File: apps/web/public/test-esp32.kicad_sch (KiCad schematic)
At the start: 9 parts, among them J1 USB_5V, SW1 EN_BTN, U1 ESP32-WROOM-32, U2 AMS1117-3.3

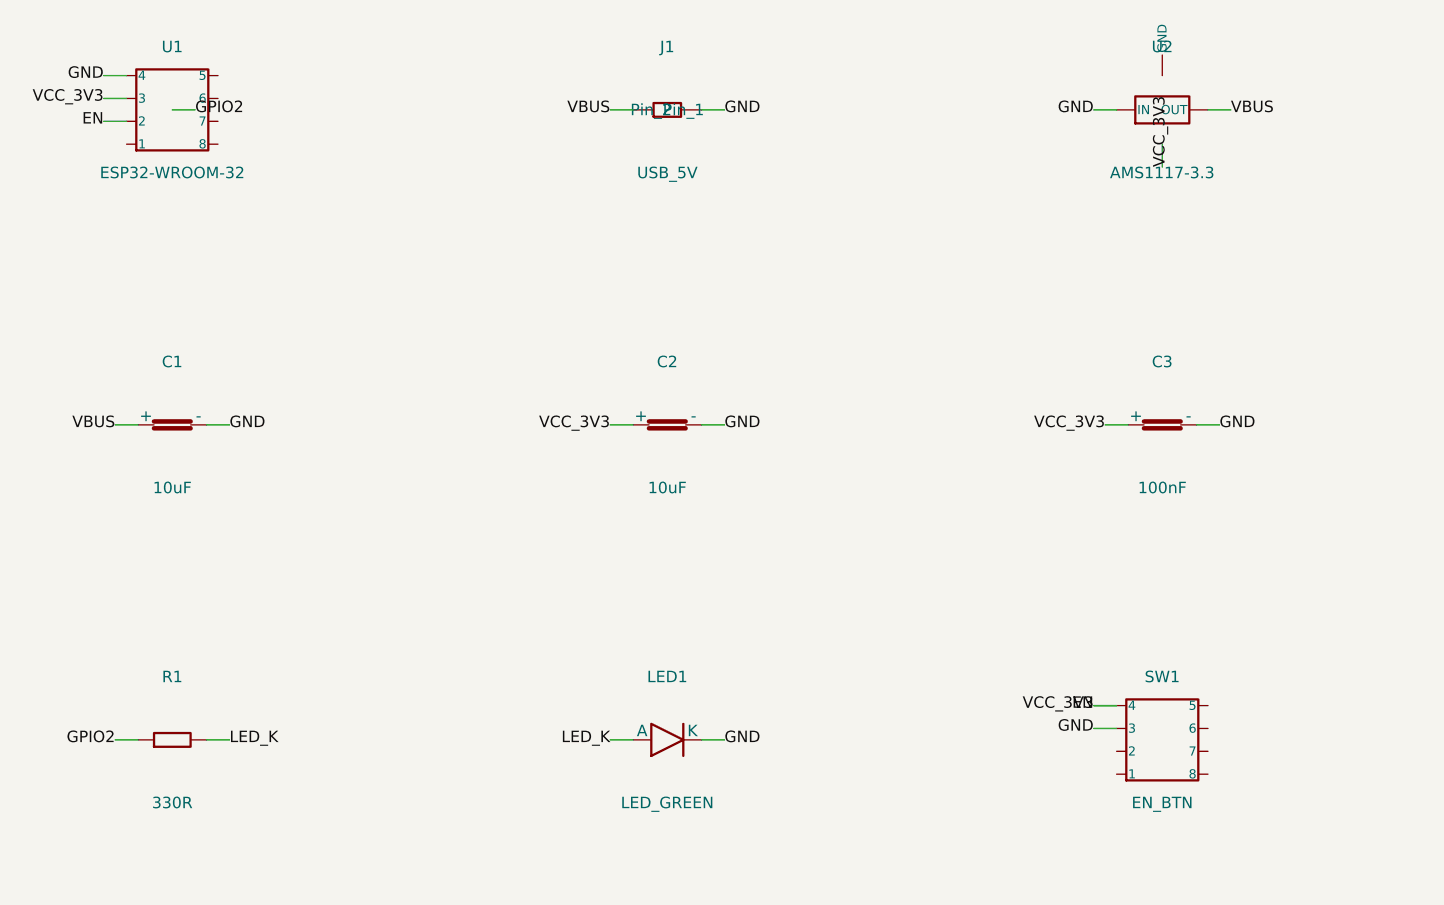
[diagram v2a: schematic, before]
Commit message: fix(layout): margin_top 12→20mm — composants 15mm du bord cadre interne
Composants étaient à y=12mm (7mm du bord interne), visuellement collés au cadre.
Maintenant à y=20mm (15mm de marge), clairement à l'intérieur du cadre.

- circuit_synth.py: margin_top = 20mm
- test-lm7805.kicad_sch: paper 149x123 (was 115)
- test-ne555.kicad_sch: paper 149x158 (was 150)
- test-esp32.kicad_sch: paper 149x158 (was 150)
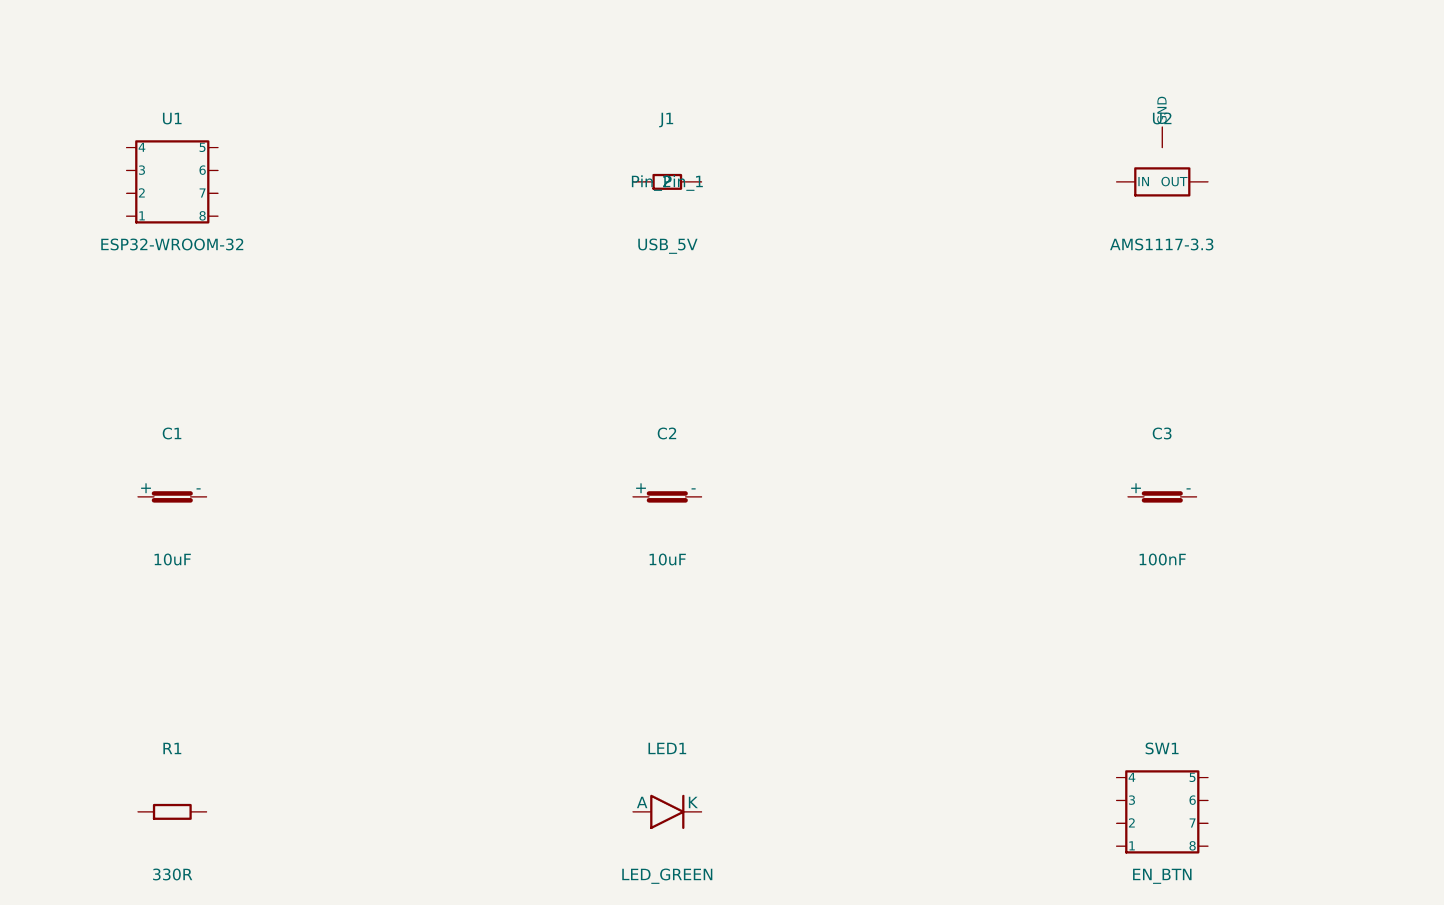
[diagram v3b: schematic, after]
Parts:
- C1, C2: footprint Capacitor_SMD:C_0805_2012Metric -> Capacitor_THT:C_Disc_D5.0mm_W2.5mm_P5.00mm
- C3: footprint Capacitor_SMD:C_0603_1608Metric -> Capacitor_THT:C_Disc_D5.0mm_W2.5mm_P5.00mm
- J1: footprint Connector_PinHeader_2.54mm:PinHeader_1x02_P2.54mm_Vertical -> Connector_USB:USB_B_Micro
- LED1: footprint LED_SMD:LED_0603_1608Metric -> LED_THT:LED_D5.0mm
- R1: footprint Resistor_SMD:R_0603_1608Metric -> Resistor_THT:R_Axial_DIN0207_L6.3mm_D2.5mm_P10.16mm_Horizontal
- SW1: footprint Button_Switch_SMD:SW_SPST_B3U-1000P -> Button_Switch_THT:SW_PUSH_6mm
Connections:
- removed net EN: C2.1 (+), C3.1 (+), SW1.4, U1.2, U1.3
- removed net GND: C1.2 (-), C2.2 (-), C3.2 (-), J1.2 (Pin_2), LED1.2 (K), SW1.3, U1.4, U2.1 (IN)
- net GPIO2: no longer names the net of R1.1
- net LED_K: no longer names the net of LED1.1 (A)
- net LED_K: no longer R1.2
- removed net VBUS: C1.1 (+), J1.1 (Pin_1), U2.3 (OUT)

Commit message: fix(schematic): add 20mm side margin to clear inner frame border
Components U1/J1 (left column) and far-right components were drawn
on top of the KiCad inner frame vertical borders (at x=10mm from
paper edge). The previous 12mm margin_side only gave 2mm clearance.

Changes:
- margin_side 12 -> 20mm in _build_flat_schematic_with_net_labels()
  (gives 10mm clearance from inner frame on both sides)
- Regenerated test-lm7805 / test-ne555 / test-esp32 .kicad_sch via
  /circuit-synth/generate (paper width 149 -> 165mm as a result)
- test-cs.html: ResizeObserver on canvas + window load/resize retries
  to reapply auto-zoom when KiCanvas resets its camera on layout
  changes (fixes title block peeking before click-to-interact)

Verified via Chrome DevTools screenshots on all 3 schematic tabs.
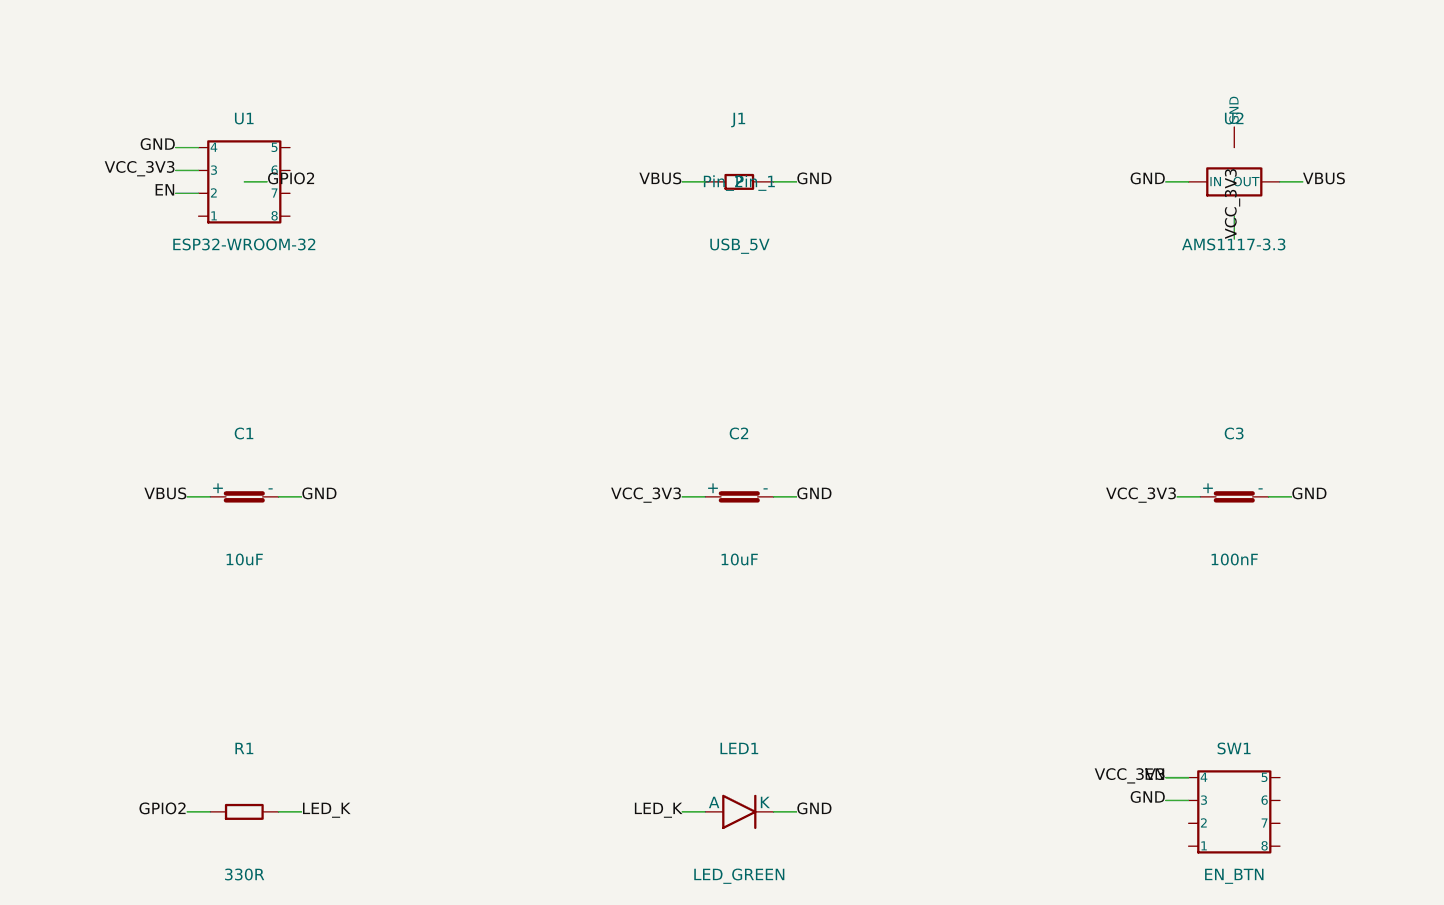
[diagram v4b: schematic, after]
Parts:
- C1, C2: footprint Capacitor_THT:C_Disc_D5.0mm_W2.5mm_P5.00mm -> Capacitor_SMD:C_0805_2012Metric
- C3: footprint Capacitor_THT:C_Disc_D5.0mm_W2.5mm_P5.00mm -> Capacitor_SMD:C_0603_1608Metric
- J1: footprint Connector_USB:USB_B_Micro -> Connector_PinHeader_2.54mm:PinHeader_1x02_P2.54mm_Vertical
- LED1: footprint LED_THT:LED_D5.0mm -> LED_SMD:LED_0603_1608Metric
- R1: footprint Resistor_THT:R_Axial_DIN0207_L6.3mm_D2.5mm_P10.16mm_Horizontal -> Resistor_SMD:R_0603_1608Metric
- SW1: footprint Button_Switch_THT:SW_PUSH_6mm -> Button_Switch_SMD:SW_SPST_B3U-1000P
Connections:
- net LED_K: now reaches LED1.1 (A)
- net LED_K: now also R1.2
- net GND: now reaches LED1.2 (K)
- net GND: now also C1.2 (-), C2.2 (-), C3.2 (-), J1.2 (Pin_2), SW1.3, U1.4, U2.1 (IN)
- net EN: now reaches SW1.4
- net EN: now also C2.1 (+), C3.1 (+), U1.2, U1.3
- net GPIO2: now reaches R1.1
- net VBUS: now reaches J1.1 (Pin_1)
- net VBUS: now also C1.1 (+), U2.3 (OUT)

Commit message: fix(schematic): bump margin_side to 28mm so net-label text stays inside frame
Previous 20mm margin put component body 10mm inside the inner frame,
but net-label text ("VIN", "VOUT", "GND"...) extends ~8mm left/right
of the body — so label text sat only ~3mm from the inner frame border,
looking cramped.

New 28mm margin_side accounts for the 8mm label overhang:
  component body at x=28mm
  label text reaches x=28-8=20mm
  inner frame at x=10mm
  -> 10mm visual clearance between label text and frame border

Paper width grows 165 -> 181mm. Regenerated all 3 test schematics.
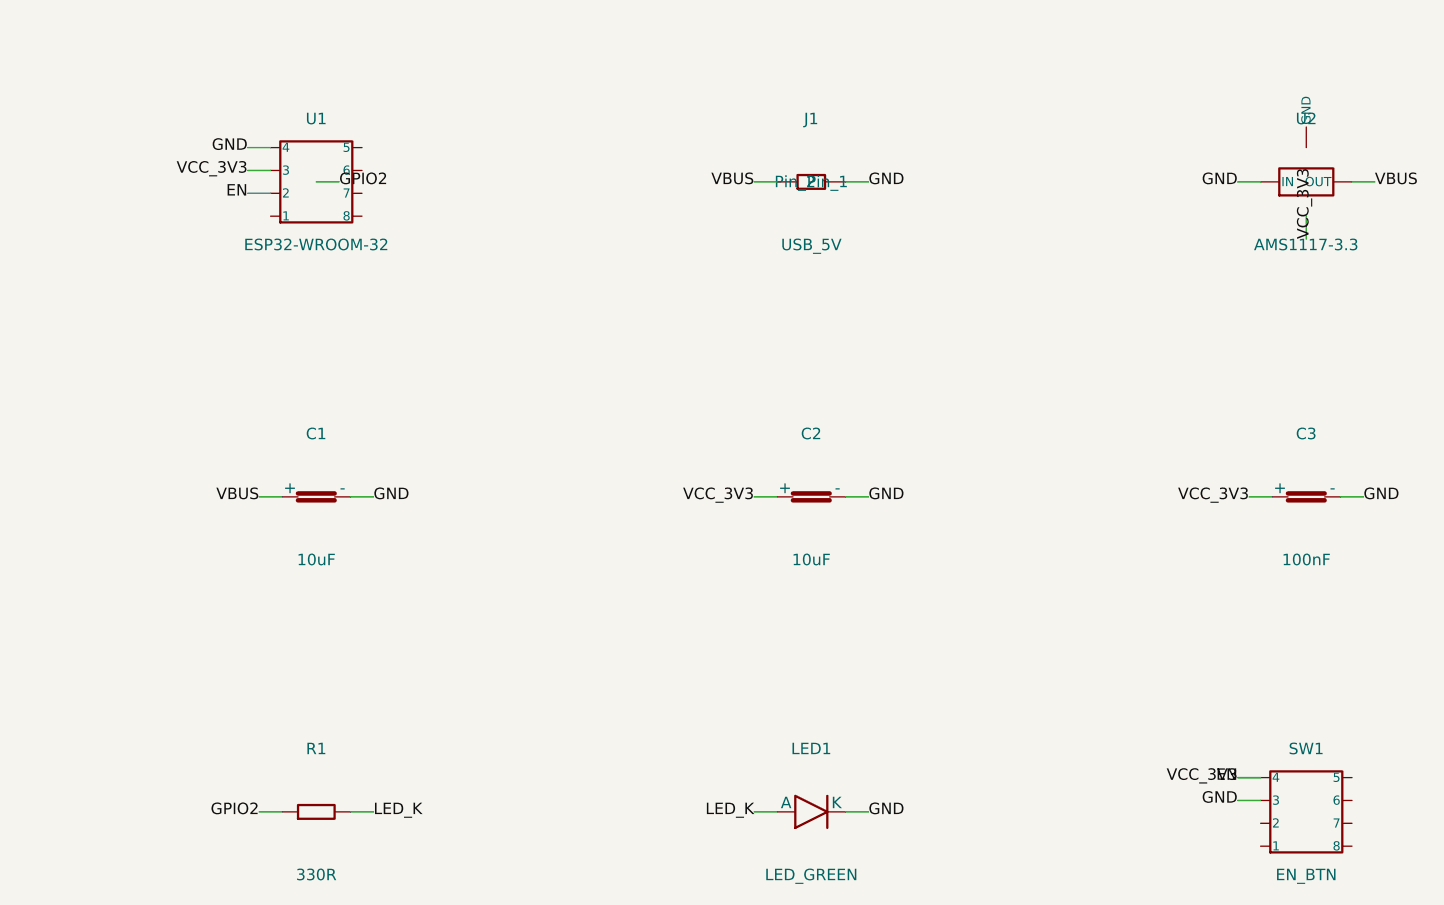
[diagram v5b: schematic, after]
